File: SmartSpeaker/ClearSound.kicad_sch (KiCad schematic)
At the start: 25 parts

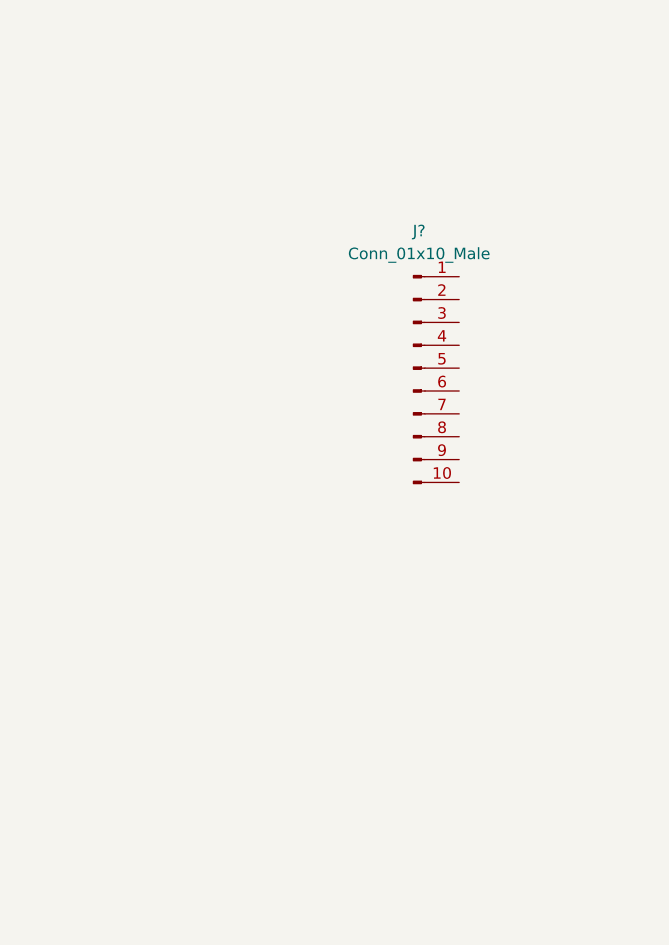
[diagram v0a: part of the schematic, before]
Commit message: UARTS added
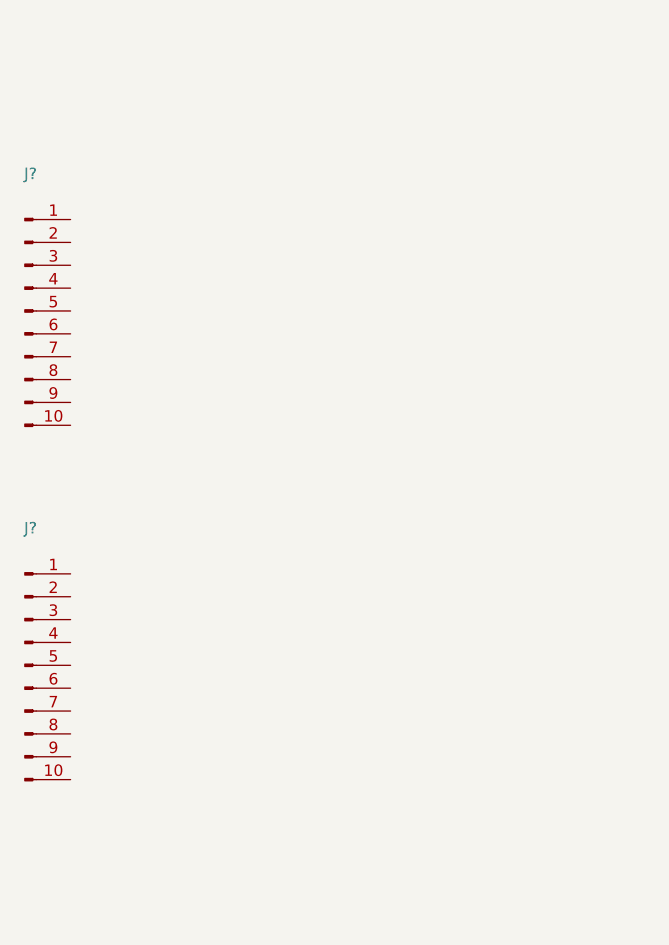
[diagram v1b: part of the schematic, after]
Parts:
- added J?: (no value), symbol Connector:Conn_01x10_Male
- J?: value Conn_01x10_Male -> (none)
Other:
- moved on the sheet: J?
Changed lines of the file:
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@@
     (pin "2")
   )
-  (symbol (lib_id "Connector:Conn_01x10_Male") (at 87.63 502.92 0) (unit 1)
-    (in_bom yes) (on_board yes) (fields_autoplaced)
-    (property "Reference" "J?" (id 0) (at 88.265 487.68 0))
-    (property "Value" "Conn_01x10_Male" (id 1) (at 88.265 490.22 0))
-    (property "Footprint" "" (id 2) (at 87.63 502.92 0)
-      (effects (font (size 1.27 1.27)) hide)
-    )
-    (property "Datasheet" "~" (id 3) (at 87.63 502.92 0)
+  (symbol (lib_id "Connector:Conn_01x10_Male") (at 44.45 496.57 0) (unit 1)
+    (in_bom yes) (on_board yes) (fields_autoplaced)
+    (property "Reference" "J?" (id 0) (at 45.085 481.33 0))
+    (property "Value" "" (id 1) (at 45.085 483.87 0))
+    (property "Footprint" "" (id 2) (at 44.45 496.57 0)
+      (effects (font (size 1.27 1.27)) hide)
+    )
+    (property "Datasheet" "~" (id 3) (at 44.45 496.57 0)
       (effects (font (size 1.27 1.27)) hide)
     )
@@
     (pin "1")
     (pin "2")
+  )
+  (symbol (lib_id "Connector:Conn_01x10_Male") (at 44.45 535.94 0) (unit 1)
+    (in_bom yes) (on_board yes) (fields_autoplaced)
+    (property "Reference" "J?" (id 0) (at 45.085 520.7 0))
+    (property "Value" "" (id 1) (at 45.085 523.24 0))
+    (property "Footprint" "" (id 2) (at 44.45 535.94 0)
+      (effects (font (size 1.27 1.27)) hide)
+    )
+    (property "Datasheet" "~" (id 3) (at 44.45 535.94 0)
+      (effects (font (size 1.27 1.27)) hide)
+    )
+    (pin "1")
+    (pin "10")
+    (pin "2")
+    (pin "3")
+    (pin "4")
+    (pin "5")
+    (pin "6")
+    (pin "7")
+    (pin "8")
+    (pin "9")
   )
   (symbol (lib_id "Device:C_Small") (at 532.13 116.84 0) (unit 1)
@@
     )
     (path "/20f2dce8-961a-4e4e-8c0c-8852ee8c26f1"
-      (reference "J?") (unit 1) (value "Conn_01x10_Male") (footprint "")
+      (reference "J?") (unit 1) (value "UART_DSP") (footprint "")
     )
     (path "/85a923bf-b61c-48f6-88ba-86956d608074"
       (reference "J?") (unit 1) (value "Conn_01x02") (footprint "")
     )
+    (path "/c91e9ad2-f8d4-4f16-9e94-92e2e0d3ea9a"
+      (reference "J?") (unit 1) (value "UART_WI-FI") (footprint "")
+    )
     (path "/dda91678-3306-4a15-b965-0a3f44087fd2"

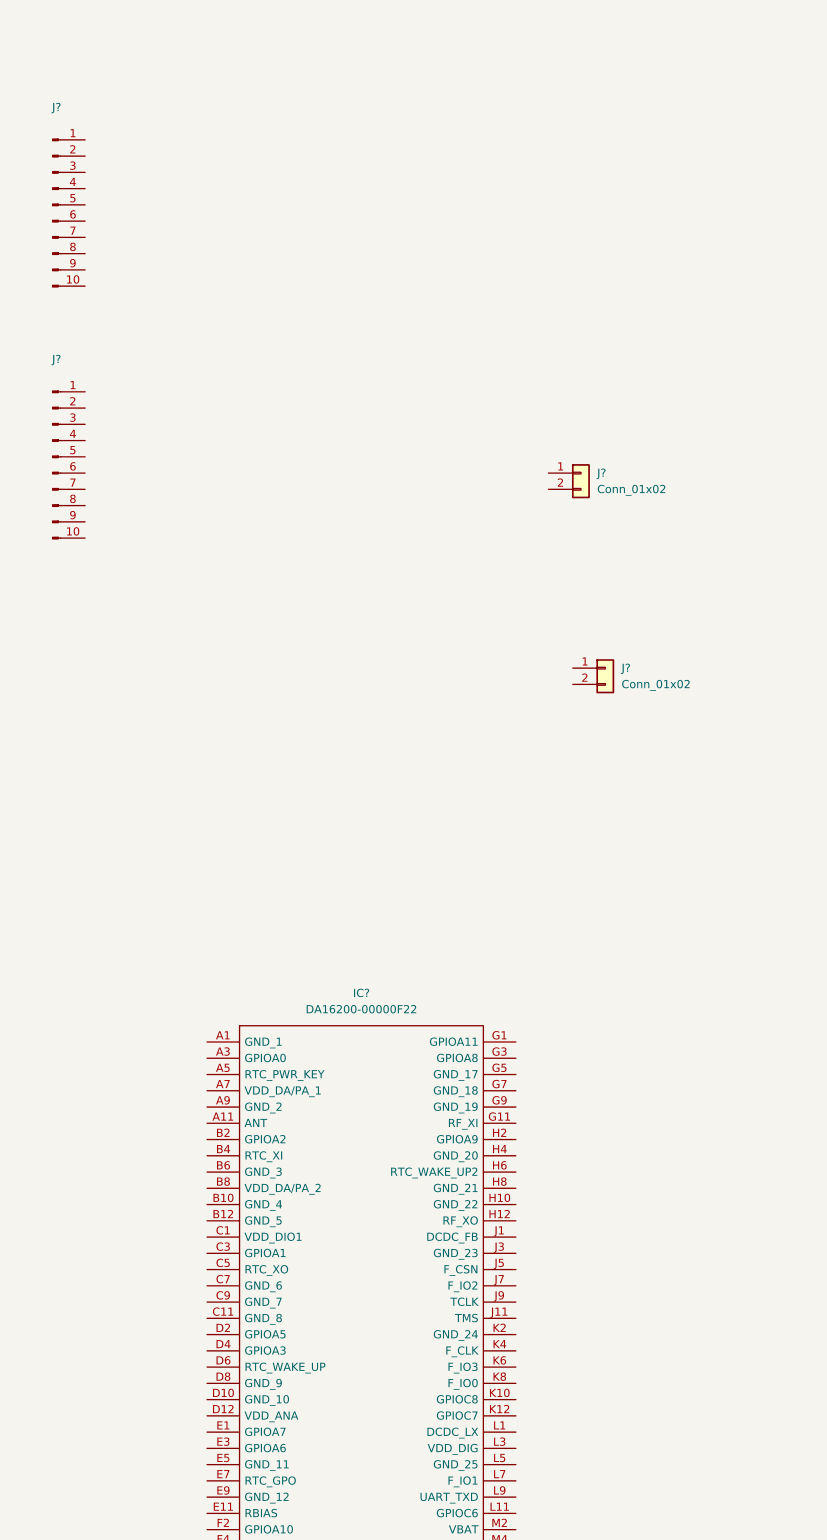
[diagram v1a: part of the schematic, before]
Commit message: Add Wi-Fi chip connection labels
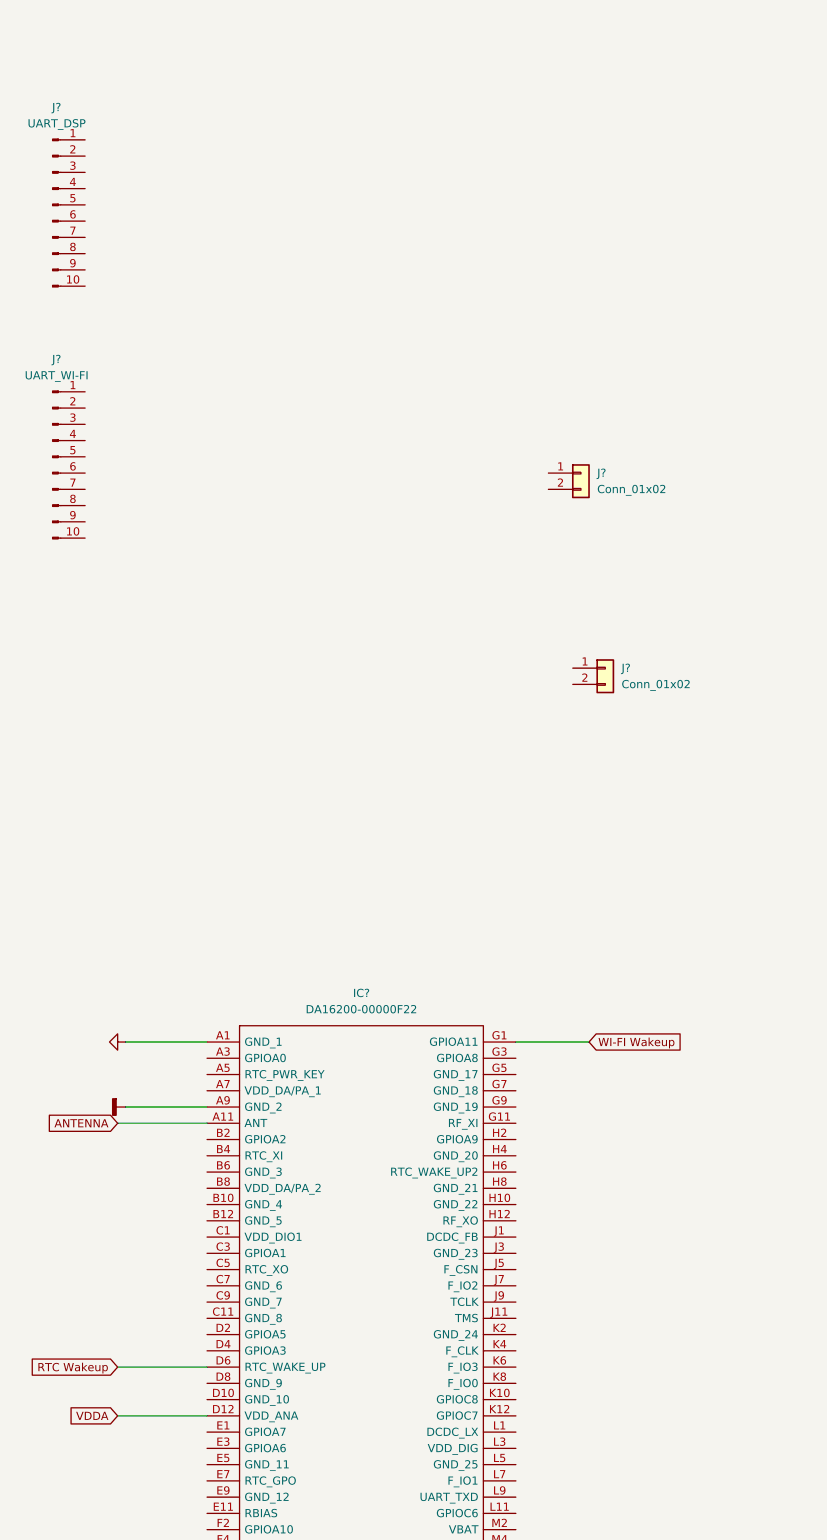
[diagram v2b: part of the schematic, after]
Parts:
- J?: value (none) -> UART_DSP
- J?: value (none) -> UART_WI-FI
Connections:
- net GND: now also IC?.A1 (GND_1)
- net ANTENNA: now reaches IC?.A11 (ANT)
- net GNDD: now reaches IC?.A9 (GND_2)
- net VDDA: now reaches IC?.D12 (VDD_ANA)
- net RTC Wakeup: now reaches IC?.D6 (RTC_WAKE_UP)
- net WI-FI Wakeup: now reaches IC?.G1 (GPIOA11)
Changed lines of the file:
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@@
+    (stroke (width 0) (type default) (color 0 0 0 0))
+  )
+  (wire (pts (xy 55.88 627.38) (xy 68.58 627.38))
     (stroke (width 0) (type default) (color 0 0 0 0))
   )
@@
     (stroke (width 0) (type default) (color 0 0 0 0))
   )
+  (wire (pts (xy 116.84 627.38) (xy 128.27 627.38))
+    (stroke (width 0) (type default) (color 0 0 0 0))
+  )
   (wire (pts (xy 492.76 60.96) (xy 508 60.96))
     (stroke (width 0) (type default) (color 0 0 0 0))
@@
     (stroke (width 0) (type default) (color 0 0 0 0))
   )
+  (wire (pts (xy 54.61 640.08) (xy 68.58 640.08))
+    (stroke (width 0) (type default) (color 0 0 0 0))
+  )
   (wire (pts (xy 483.87 55.88) (xy 491.49 55.88))
     (stroke (width 0) (type default) (color 0 0 0 0))
@@
     (stroke (width 0) (type default) (color 0 0 0 0))
   )
+  (wire (pts (xy 55.88 637.54) (xy 68.58 637.54))
+    (stroke (width 0) (type default) (color 0 0 0 0))
+  )
   (wire (pts (xy 519.43 119.38) (xy 519.43 127))
     (stroke (width 0) (type default) (color 0 0 0 0))
@@
   )
   (wire (pts (xy 490.22 86.36) (xy 483.87 86.36))
+    (stroke (width 0) (type default) (color 0 0 0 0))
+  )
+  (wire (pts (xy 54.61 685.8) (xy 68.58 685.8))
+    (stroke (width 0) (type default) (color 0 0 0 0))
+  )
+  (wire (pts (xy 54.61 678.18) (xy 68.58 678.18))
     (stroke (width 0) (type default) (color 0 0 0 0))
   )
@@
     )
   )
+  (global_label "ANTENNA" (shape input) (at 54.61 640.08 180) (fields_autoplaced)
+    (effects (font (size 1.27 1.27)) (justify right))
+    (property "Intersheet References" "${INTERSHEET_REFS}" (id 0) (at 43.9117 640.0006 0)
+      (effects (font (size 1.27 1.27)) (justify right) hide)
+    )
+  )
+  (global_label "VDDA" (shape input) (at 54.61 685.8 180) (fields_autoplaced)
+    (effects (font (size 1.27 1.27)) (justify right))
+    (property "Intersheet References" "${INTERSHEET_REFS}" (id 0) (at 47.4798 685.7206 0)
+      (effects (font (size 1.27 1.27)) (justify right) hide)
+    )
+  )
   (global_label "AVCC" (shape input) (at 504.19 137.16 0) (fields_autoplaced)
     (effects (font (size 1.27 1.27)) (justify left))
@@
     (effects (font (size 1.27 1.27)) (justify right))
     (property "Intersheet References" "${INTERSHEET_REFS}" (id 0) (at 427.2098 68.6594 0)
+      (effects (font (size 1.27 1.27)) (justify right) hide)
+    )
+  )
+  (global_label "WI-FI Wakeup" (shape input) (at 128.27 627.38 0) (fields_autoplaced)
+    (effects (font (size 1.27 1.27)) (justify left))
+    (property "Intersheet References" "${INTERSHEET_REFS}" (id 0) (at 143.9879 627.3006 0)
+      (effects (font (size 1.27 1.27)) (justify left) hide)
+    )
+  )
+  (global_label "RTC Wakeup" (shape input) (at 54.61 678.18 180) (fields_autoplaced)
+    (effects (font (size 1.27 1.27)) (justify right))
+    (property "Intersheet References" "${INTERSHEET_REFS}" (id 0) (at 40.7064 678.1006 0)
       (effects (font (size 1.27 1.27)) (justify right) hide)
     )
@@
     (in_bom yes) (on_board yes) (fields_autoplaced)
     (property "Reference" "J?" (id 0) (at 45.085 481.33 0))
-    (property "Value" "" (id 1) (at 45.085 483.87 0))
+    (property "Value" "UART_DSP" (id 1) (at 45.085 483.87 0))
     (property "Footprint" "" (id 2) (at 44.45 496.57 0)
       (effects (font (size 1.27 1.27)) hide)
@@
     (pin "2")
   )
+  (symbol (lib_id "power:GNDD") (at 55.88 637.54 270) (unit 1)
+    (in_bom yes) (on_board yes) (fields_autoplaced)
+    (property "Reference" "#PWR?" (id 0) (at 49.53 637.54 0)
+      (effects (font (size 1.27 1.27)) hide)
+    )
+    (property "Value" "" (id 1) (at 52.07 637.5399 90)
+      (effects (font (size 1.27 1.27)) (justify right))
+    )
+    (property "Footprint" "" (id 2) (at 55.88 637.54 0)
+      (effects (font (size 1.27 1.27)) hide)
+    )
+    (property "Datasheet" "" (id 3) (at 55.88 637.54 0)
+      (effects (font (size 1.27 1.27)) hide)
+    )
+    (pin "1")
+  )
   (symbol (lib_id "Device:C_Small") (at 532.13 158.75 0) (unit 1)
     (in_bom yes) (on_board yes) (fields_autoplaced)
@@
     (pin "1")
     (pin "2")
+  )
+  (symbol (lib_id "power:GND") (at 55.88 627.38 270) (unit 1)
+    (in_bom yes) (on_board yes) (fields_autoplaced)
+    (property "Reference" "#PWR?" (id 0) (at 49.53 627.38 0)
+      (effects (font (size 1.27 1.27)) hide)
+    )
+    (property "Value" "" (id 1) (at 52.07 627.3799 90)
+      (effects (font (size 1.27 1.27)) (justify right))
+    )
+    (property "Footprint" "" (id 2) (at 55.88 627.38 0)
+      (effects (font (size 1.27 1.27)) hide)
+    )
+    (property "Datasheet" "" (id 3) (at 55.88 627.38 0)
+      (effects (font (size 1.27 1.27)) hide)
+    )
+    (pin "1")
   )
   (symbol (lib_id "Device:C_Small") (at 528.32 82.55 0) (unit 1)
@@
     (in_bom yes) (on_board yes) (fields_autoplaced)
     (property "Reference" "J?" (id 0) (at 45.085 520.7 0))
-    (property "Value" "" (id 1) (at 45.085 523.24 0))
+    (property "Value" "UART_WI-FI" (id 1) (at 45.085 523.24 0))
     (property "Footprint" "" (id 2) (at 44.45 535.94 0)
       (effects (font (size 1.27 1.27)) hide)
@@
       (reference "#PWR?") (unit 1) (value "GND") (footprint "")
     )
+    (path "/25a41a07-1570-4934-8650-4f8da365f679"
+      (reference "#PWR?") (unit 1) (value "GNDD") (footprint "")
+    )
+    (path "/4a7017bb-a698-433b-a0be-587786fcc0bb"
+      (reference "#PWR?") (unit 1) (value "GND") (footprint "")
+    )

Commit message: Evgenii's last changes
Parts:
- removed C? (x5): 0.1µF, symbol Device:C_Small
- removed C? (x2): 100µF, symbol Device:C_Polarized_Small_US
- removed C?: 1µF, symbol Device:C_Small
- removed C? (x2): 0.47µF, symbol Device:C_Small
- removed C? (x2): 0.68µF, symbol Device:C_Small
- removed C? (x2): 1000pF, symbol Device:C_Small
- removed IC?: TPA3138D2PWPR, SOP65P640X120-29N, symbol AMP:TPA3138D2PWPR
- removed L? (x2): 10µH, symbol Device:L_Iron
- removed LS?: Speaker, symbol Device:Speaker
- removed R?: 39kΩ, symbol Device:R_Small
- removed R?: 51k Ω, symbol Device:R_Small
- added C? (x2): 0.68µF, symbol Device:C_Small
- added C? (x2): 0.47µF, symbol Device:C_Small
- added C? (x5): 0.1µF, symbol Device:C_Small
- added C? (x2): 100µF, symbol Device:C_Polarized_Small_US
- added C? (x2): 1000pF, symbol Device:C_Small
- added C?: 1µF, symbol Device:C_Small
- added IC?: TPA3138D2PWPR, SOP65P640X120-29N, symbol AMP:TPA3138D2PWPR
- added L? (x2): 10µH, symbol Device:L_Iron
- added LS?: Speaker, symbol Device:Speaker
- added R? (x3): 100kΩ, symbol Device:R_Small
- added R?: 39kΩ, symbol Device:R_Small
- added R?: 51k Ω, symbol Device:R_Small
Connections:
- net GND: now also C?.1, C?.2, C?.2, C?.2, C?.2, C?.2, C?.2, C?.2, C?.2, C?.2, C?.2, IC?.14 (AGND), IC?.19 (GND_2), IC?.24 (GND_3), IC?.29 (THERMAL_PAD), IC?.3 (LINP), IC?.4 (LINN), IC?.8 (GND_1), R?.1
- net VDD: now also C?.1, C?.1, C?.1, C?.1, C?.1, C?.1, C?.1, IC?.15 (PVCCR_1), IC?.16 (PVCCR_2), IC?.27 (PVCCL_1), IC?.28 (PVCCL_2), IC?.7 (AVCC), R?.1, R?.1, R?.1
- new net: C?.1, L?.2, LS?.2
- new net: IC?.10 (PLIMIT), R?.1, R?.2
- new net: C?.1, IC?.11 (RINN)
- new net: C?.1, IC?.12 (RINP)
- new net: C?.1, IC?.17 (BSPR), IC?.21 (BSNR)
- new net: C?.2, IC?.18 (OUTPR), IC?.20 (OUTNR), L?.1
- new net: C?.1, IC?.22 (BSNL), IC?.26 (BSPL)
- new net: C?.2, IC?.23 (OUTNL), IC?.25 (OUTPL), L?.1
- new net: IC?.5 (GAIN_SEL), R?.2
- new net: IC?.6 (MODE_SEL), R?.2
- new net: C?.2, IC?.9 (GVDD), R?.2
- new net: C?.1, L?.2, LS?.1
- new net DSP OUT: C?.2
- new net SHUTDOWN: IC?.2 (~{SD}/~{FAULT}), R?.2
